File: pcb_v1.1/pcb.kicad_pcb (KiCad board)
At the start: 2 copper layers, 65 x 45 mm, 42 parts, among them J1 Screw_Terminal_01x02, J2 Screw_Terminal_01x02, J3 Screw_Terminal_01x02, J4 Screw_Terminal_01x02, J5 Screw_Terminal_01x02, J6 Screw_Terminal_01x02, SW1 SW_Push_Dual, U1 STM32F072C8Tx, U2 MAX31865, U3 LM7805_TO220, U4 AMS1117-3.3

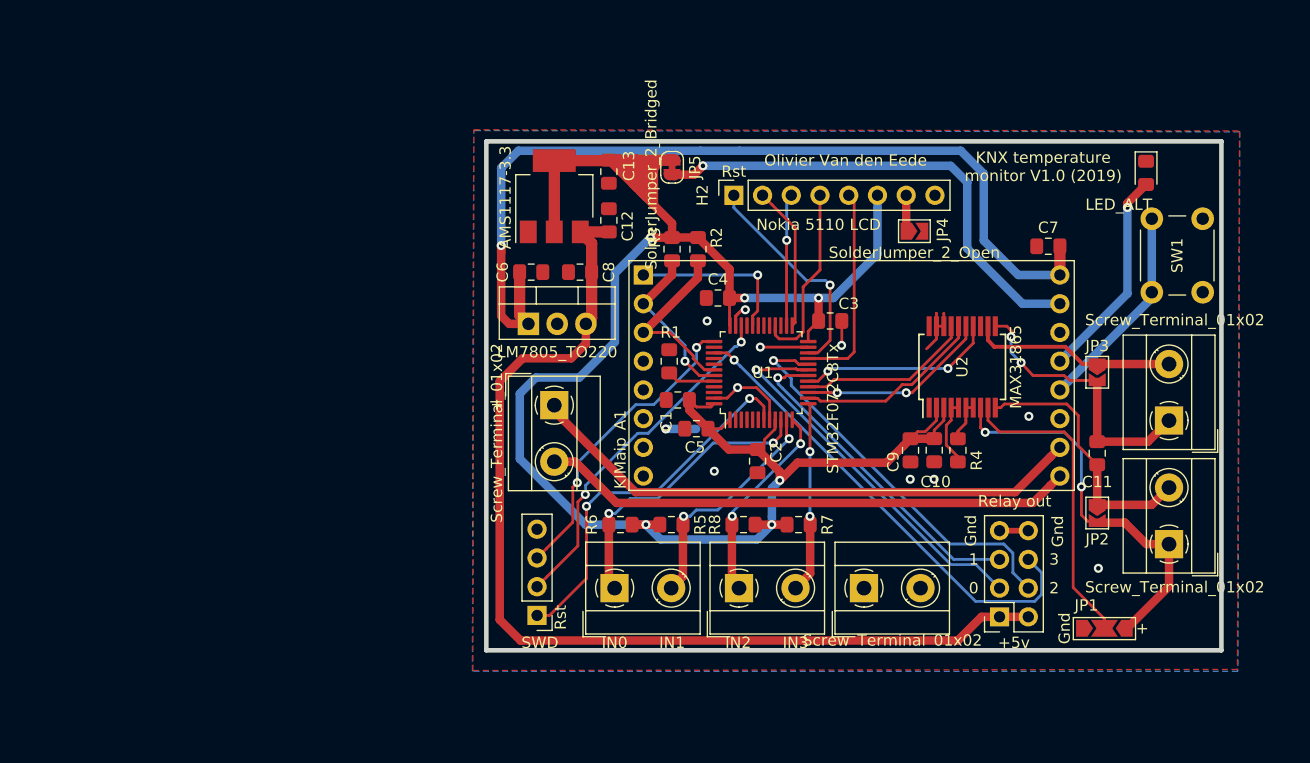
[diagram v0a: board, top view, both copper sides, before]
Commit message: pcb v1.1 component placement
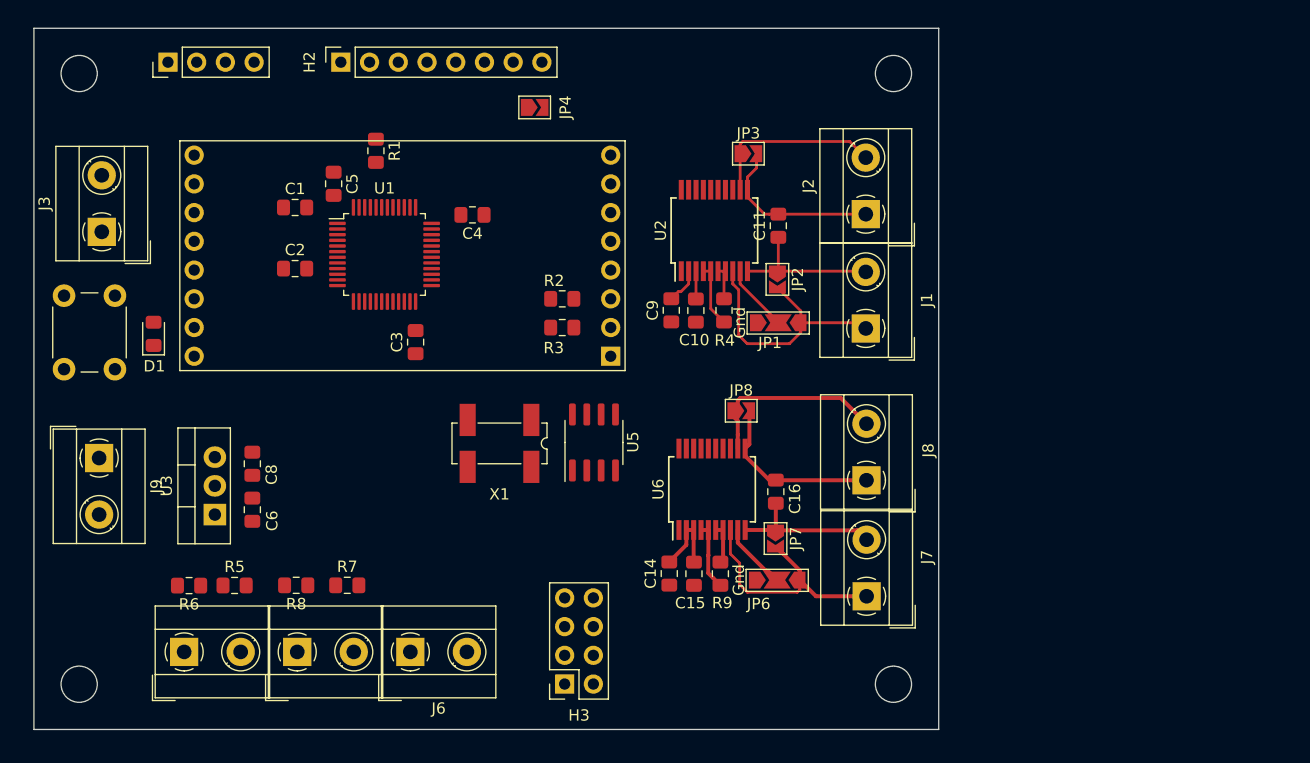
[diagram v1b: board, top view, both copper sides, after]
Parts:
- removed C12, C13: 1uf, Capacitor_SMD:C_0805_2012Metric_Pad1.15x1.40mm_HandSolder
- removed C7: 0.1uf, Capacitor_SMD:C_0805_2012Metric_Pad1.15x1.40mm_HandSolder
- removed JP5: SolderJumper_2_Bridged, Jumper:SolderJumper-2_P1.3mm_Bridged_RoundedPad1.0x1.5mm
- removed U4: AMS1117-3.3, Package_TO_SOT_SMD:SOT-223-3_TabPin2
- added C14: 0.1uf, Capacitor_SMD:C_0805_2012Metric_Pad1.15x1.40mm_HandSolder, F.Cu at (106.2, 78.2)
- added C15: 0.1uf, Capacitor_SMD:C_0805_2012Metric_Pad1.15x1.40mm_HandSolder, F.Cu at (108.4, 78.2)
- added C16: 0.1uf, Capacitor_SMD:C_0805_2012Metric_Pad1.15x1.40mm_HandSolder, F.Cu at (115.6, 71.0)
- added J7: Screw_Terminal_01x02, TerminalBlock_MetzConnect:TerminalBlock_MetzConnect_Type055_RT01502HDWU_1x02_P5.00mm_Horizontal, F.Cu at (123.6, 80.2)
- added J8: Screw_Terminal_01x02, TerminalBlock_MetzConnect:TerminalBlock_MetzConnect_Type055_RT01502HDWU_1x02_P5.00mm_Horizontal, F.Cu at (123.6, 70.0)
- added J9: Screw_Terminal_01x02, TerminalBlock_MetzConnect:TerminalBlock_MetzConnect_Type055_RT01502HDWU_1x02_P5.00mm_Horizontal, F.Cu at (55.8, 68.0)
- added JP6: SolderJumper_3_Open, Jumper:SolderJumper-3_P2.0mm_Open_TrianglePad1.0x1.5mm_NumberLabels, F.Cu at (115.7, 78.8)
- added JP7: SolderJumper_2_Open, Jumper:SolderJumper-2_P1.3mm_Open_TrianglePad1.0x1.5mm, F.Cu at (115.6, 75.1)
- added JP8: SolderJumper_2_Open, Jumper:SolderJumper-2_P1.3mm_Open_TrianglePad1.0x1.5mm, F.Cu at (112.5, 63.8)
- added R9: 420, Resistor_SMD:R_0805_2012Metric_Pad1.15x1.40mm_HandSolder, F.Cu at (110.7, 78.2)
- added REF**: MountingHole_3.2mm_M3, MountingHole:MountingHole_3.2mm_M3, F.Cu at (54.0, 88.0)
- added REF**: MountingHole_3.2mm_M3, MountingHole:MountingHole_3.2mm_M3, F.Cu at (126.0, 88.0)
- added REF**: MountingHole_3.2mm_M3, MountingHole:MountingHole_3.2mm_M3, F.Cu at (126.0, 34.0)
- added REF**: MountingHole_3.2mm_M3, MountingHole:MountingHole_3.2mm_M3, F.Cu at (54.0, 34.0)
- added U5: DS1307Z+, Package_SO:SOIC-8_3.9x4.9mm_P1.27mm, F.Cu at (99.5, 66.6)
- added U6: MAX31865, Package_SO:SSOP-20_5.3x7.2mm_P0.65mm, F.Cu at (110.0, 70.8)
- added X1: 32.768kHz, Crystal:Crystal_SMD_SeikoEpson_MC306-4Pin_8.0x3.2mm_HandSoldering, F.Cu at (91.2, 66.7)
- moved SW1 91.7 mm to (57.2, 53.6), turned to 270 degrees
- moved D1 88.9 mm to (60.6, 57.0), turned to 90 degrees
- moved H1 58.8 mm to (61.8, 33.0), turned to 90 degrees
- moved C2 44.3 mm to (73.1, 51.2), turned to 0 degrees
- moved J3 42.8 mm to (56.0, 48.0), turned to 90 degrees
- moved J6 40.5 mm to (83.3, 85.1)
- moved R7 40.3 mm to (77.7, 79.3)
- moved R8 39.9 mm to (73.2, 79.3)
- moved JP1 39.5 mm to (115.8, 56.0)
- moved J5 39.5 mm to (73.3, 85.1)
- moved R5 39.0 mm to (67.7, 79.3)
- moved H3 38.9 mm to (96.9, 88.0)
- moved C5 38.7 mm to (76.5, 43.8), turned to 270 degrees
- moved R6 38.5 mm to (63.7, 79.3)
- moved J4 38.5 mm to (63.3, 85.1)
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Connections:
- A1 pad 15: Net-(A1-Pad15) -> +3V3
- A1 pad 16: +12V -> Net-(A1-Pad16)
- C6 pad 2: +12V -> +24V
- U1 pad 14: /SS_1 -> /OUT_0
- U1 pad 15: /CLK_1 -> /OUT_1
- U1 pad 16: /MISO_1 -> /OUT_3
- U1 pad 17: /MOSI_1 -> /OUT_2
- U1 pad 18: /OUT_1 -> Net-(U1-Pad18)
- U1 pad 19: /OUT_0 -> Net-(U1-Pad19)
- U1 pad 20: /OUT_2 -> Net-(U1-Pad20)
- U1 pad 21: /LCD_CLK -> /DRDY
- U1 pad 22: /LCD_RST -> /SDA
- U1 pad 25: /LCD_CE -> Net-(U1-Pad25)
- U1 pad 26: /LCD_DC -> /SCL
- U1 pad 27: Net-(U1-Pad27) -> /SS_2
- U1 pad 28: /LCD_DATA -> /MOSI_1
- U1 pad 29: Net-(U1-Pad29) -> /CLK_1
- U1 pad 30: Net-(U1-Pad30) -> /SS_1
- U1 pad 31: Net-(U1-Pad31) -> /MISO_1
- U1 pad 32: /DRDY -> Net-(U1-Pad32)
- U1 pad 39: /OUT_3 -> Net-(U1-Pad39)
- U1 pad 41: Net-(U1-Pad41) -> /LCD_CLK
- U1 pad 42: /SCL -> /LCD_DATA
- U1 pad 43: /SDA -> /LCD_DC
- U1 pad 45: Net-(U1-Pad45) -> /LCD_CE
- U1 pad 46: Net-(U1-Pad46) -> /LCD_RST
- U3 pad 1: +12V -> +24V
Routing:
- net +3V3: track 189.2 -> 12.6 mm, vias 6 -> 0
- net +5V: track 91.5 -> 0.00 mm
- net +12V: track 82.0 -> 0.00 mm, vias 1 -> 0
- net GND: track 74.3 -> 0.00 mm, vias 11 -> 0
- net Net-(A1-Pad10): track 49.8 -> 0.00 mm
- net Net-(A1-Pad15): track 43.2 -> 0.00 mm, vias 1 -> 0
- net /OUT_3: track 41.9 -> 0.00 mm, vias 1 -> 0
- net /OUT_2: track 35.5 -> 0.00 mm, vias 1 -> 0
- net /OUT_0: track 34.2 -> 0.00 mm, vias 1 -> 0
- net /NRST: track 33.2 -> 0.00 mm, vias 2 -> 0
- net /SWDIO: track 31.2 -> 0.00 mm, vias 2 -> 0
- net /OUT_1: track 29.3 -> 0.00 mm, vias 1 -> 0
- net /SWDCLK: track 27.1 -> 0.00 mm, vias 2 -> 0
- net /BIN_0: track 27.0 -> 0.00 mm, vias 2 -> 0
- net Net-(J7-Pad1): track 0.00 -> 22.1 mm
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- removed copper zone on B.Cu, net GND
- removed copper zone on F.Cu, net GND
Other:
- board size 65 x 45 mm -> 80 x 62 mm
- board text removed: "+"
- board text removed: "+5v"
- board text removed: "-"
- board text removed: "0"
- board text removed: "1"
- board text removed: "2"
- board text removed: "3"
- board text removed: "Gnd"
- board text removed: "IN0"
- board text removed: "IN1"
- board text removed: "IN2"
- board text removed: "IN3"
- board text removed: "KNX temperature monitor V1.0 (2019)"
- board text removed: "Olivier Van den Eede"
- board text removed: "Rst"

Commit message: pcb done
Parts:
- removed J3, J9: Screw_Terminal_01x02, TerminalBlock_MetzConnect:TerminalBlock_MetzConnect_Type055_RT01502HDWU_1x02_P5.00mm_Horizontal
- added 24V: 24v, TerminalBlock_MetzConnect:TerminalBlock_MetzConnect_Type055_RT01502HDWU_1x02_P5.00mm_Horizontal, F.Cu at (56.0, 68.0)
- added Knx: Knx, TerminalBlock_MetzConnect:TerminalBlock_MetzConnect_Type055_RT01502HDWU_1x02_P5.00mm_Horizontal, F.Cu at (56.0, 48.0)
- Relay out: renamed from H3
- Temp +: renamed from J1
- Temp +: renamed from J7
- Temp -: renamed from J2
- Temp -: renamed from J8
- moved JP8 1.08 mm to (113.6, 64.0)
- moved C3 0.68 mm to (84.4, 57.7)
- moved R1 0.62 mm to (80.8, 40.8)
- moved C2 0.61 mm to (72.5, 51.3)
- moved JP4 0.26 mm to (94.0, 37.0)
- renumbered J6 to Common, H2 to LCD, D1 to Led, H1 to SWD
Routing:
- net +3V3: track 12.6 -> 227.3 mm, vias 0 -> 8
- net +5V: track 0.00 -> 91.3 mm, vias 0 -> 1
- net /MISO_1: track 0.00 -> 51.3 mm, vias 0 -> 2
- net /MOSI_1: track 0.00 -> 49.2 mm, vias 0 -> 2
- net /CLK_1: track 0.00 -> 48.4 mm, vias 0 -> 2
- net /OUT_2: track 0.00 -> 45.0 mm
- net /OUT_3: track 0.00 -> 42.3 mm
- net /BIN_0: track 0.00 -> 42.1 mm
- net GND: track 0.00 -> 40.8 mm, vias 0 -> 8
- net /OUT_0: track 0.00 -> 38.8 mm
- net /BIN_3: track 0.00 -> 37.0 mm
- net /BIN_1: track 0.00 -> 36.9 mm
- net /SS_2: track 0.00 -> 36.7 mm, vias 0 -> 2
- net /OUT_1: track 0.00 -> 36.1 mm
- net /BIN_2: track 0.00 -> 34.8 mm
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- added copper zone on B.Cu, net GND
- added copper zone on F.Cu, net GND
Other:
- board text added: "+"
- board text added: "+5v"
- board text added: "-"
- board text added: "0"
- board text added: "1"
- board text added: "2"
- board text added: "3"
- board text added: "Clk"
- board text added: "Data"
- board text added: "Gnd"
- board text added: "IN0"
- board text added: "IN1"
- board text added: "IN2"
- board text added: "IN3"
- board text added: "KNX temperature monitor V1.1 (2019)"
- board text added: "Lcd backlight"
- board text added: "Olivier Van den Eede"
- board text added: "Outdoor temp"
- board text added: "Ovde.be"
- board text added: "Rst"
- board text added: "Water temp"
